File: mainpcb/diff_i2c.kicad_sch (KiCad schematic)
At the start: 21 parts, among them J6 Conn_01x08, J7 Conn_01x08, J8 Conn_01x03, U5 PCA9615DP, U6 PCA9615DP

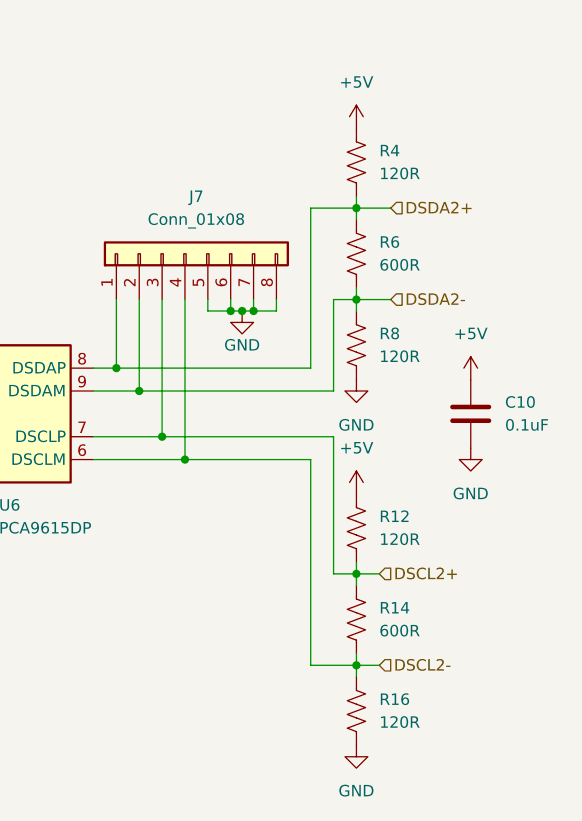
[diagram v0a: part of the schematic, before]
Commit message: Updated differential termination resistor values
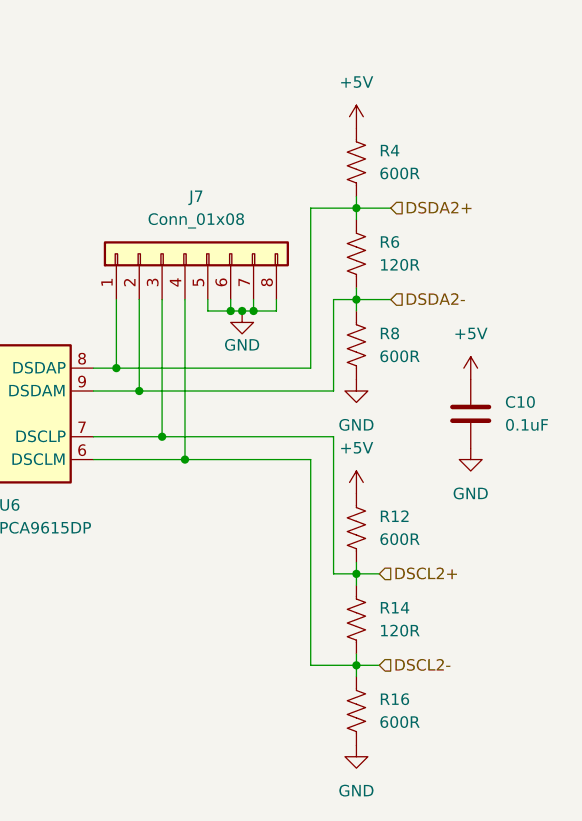
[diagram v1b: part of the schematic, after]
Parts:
- R12, R16, R4, R8: value 120R -> 600R
- R14, R6: value 600R -> 120R
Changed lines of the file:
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@@
 			)
 		)
-		(property "Value" "120R"
+		(property "Value" "600R"
 			(at 236.22 105.4099 0)
 			(effects
@@
 			)
 		)
-		(property "Value" "600R"
+		(property "Value" "120R"
 			(at 236.22 115.5699 0)
 			(effects
@@
 			)
 		)
-		(property "Value" "120R"
+		(property "Value" "600R"
 			(at 236.22 85.0899 0)
 			(effects
@@
 			)
 		)
-		(property "Value" "600R"
+		(property "Value" "120R"
 			(at 236.22 74.9299 0)
 			(effects
@@
 			)
 		)
-		(property "Value" "120R"
+		(property "Value" "600R"
 			(at 236.22 125.7299 0)
 			(effects
@@
 			)
 		)
-		(property "Value" "120R"
+		(property "Value" "600R"
 			(at 236.22 64.7699 0)
 			(effects
